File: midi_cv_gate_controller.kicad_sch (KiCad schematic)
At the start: 1 part, among them U28 ARDUINO_PRO_MINI

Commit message: Fixed alignment of jacks and LEDs
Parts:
- renumbered U28 to U122
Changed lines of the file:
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@@
   (symbol (lib_id "My Stuff:ARDUINO_PRO_MINI_custom_2") (at 119.38 93.98 0) (unit 1)
     (in_bom yes) (on_board yes) (fields_autoplaced)
-    (property "Reference" "U28" (id 0) (at 119.38 59.5335 0))
+    (property "Reference" "U122" (id 0) (at 119.38 59.5335 0))
     (property "Value" "ARDUINO_PRO_MINI" (id 1) (at 119.38 62.3086 0))
     (property "Footprint" "My Stuff:MODULE_ARDUINO_PRO_MINI_custom_2" (id 2) (at 98.044 52.832 0)

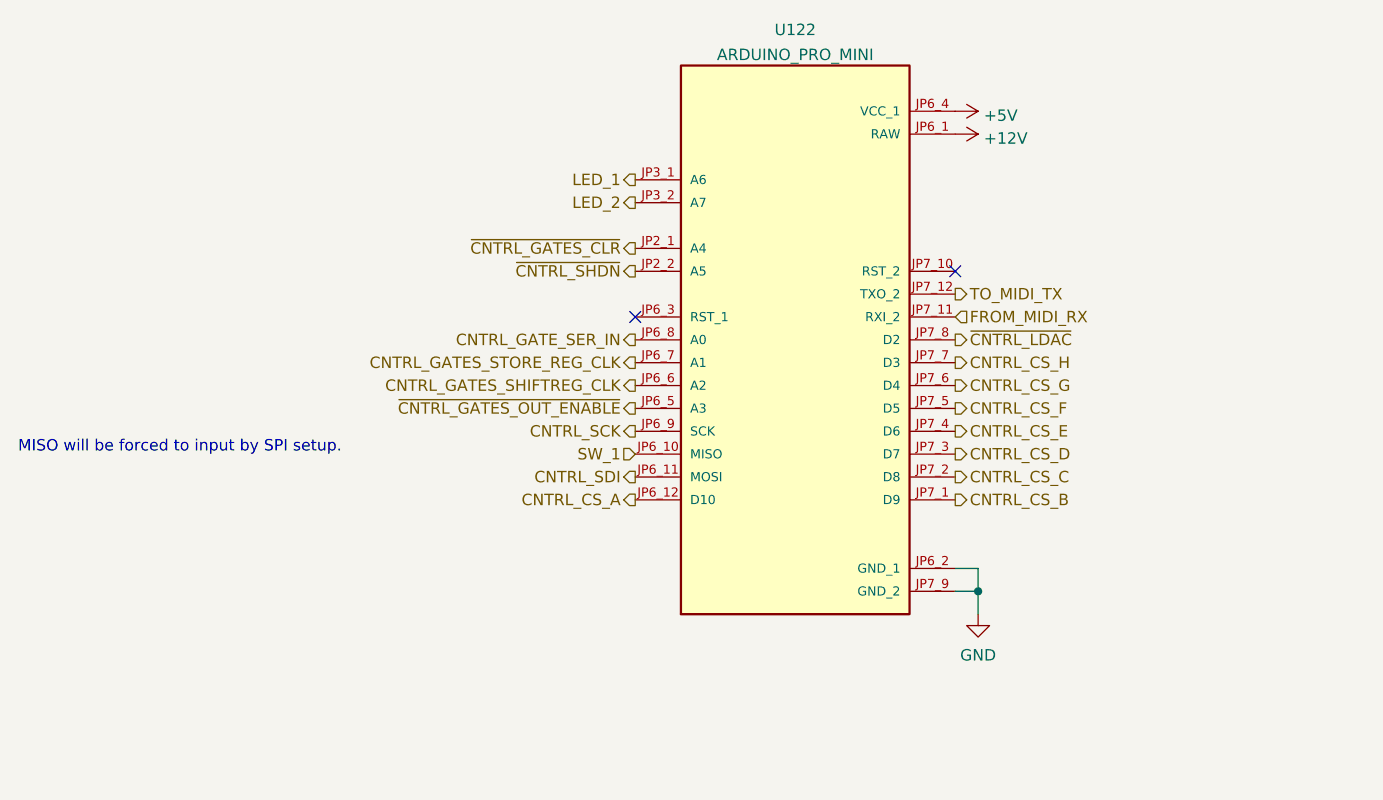
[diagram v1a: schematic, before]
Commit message: Cleanups and title blocks
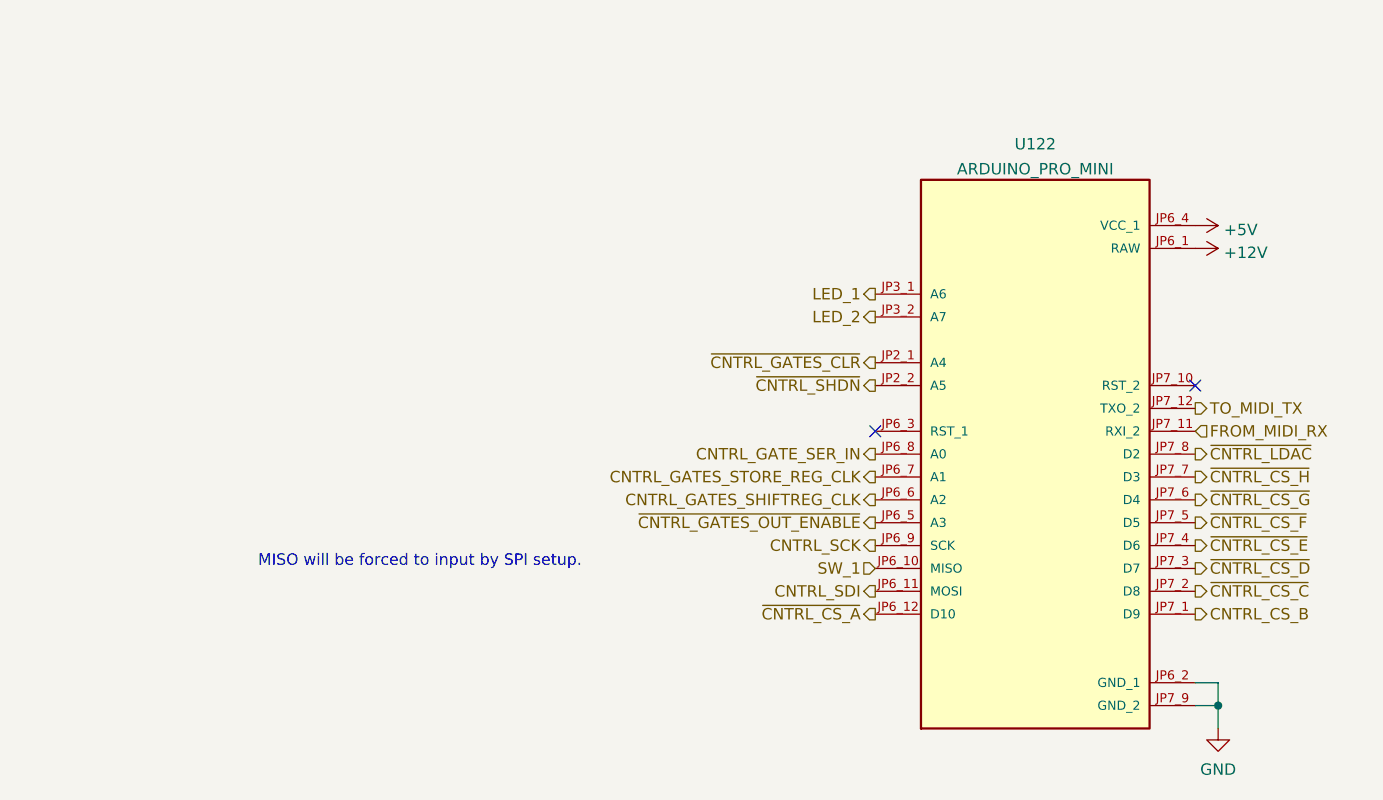
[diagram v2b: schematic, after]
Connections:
- net CNTRL_CS_A renamed ~{CNTRL_CS_A}
- net CNTRL_CS_B renamed ~{}CNTRL_CS_B
- net CNTRL_CS_C renamed ~{CNTRL_CS_C}
- net CNTRL_CS_D renamed ~{CNTRL_CS_D}
- net CNTRL_CS_E renamed ~{CNTRL_CS_E}
- net CNTRL_CS_F renamed ~{CNTRL_CS_F}
- net CNTRL_CS_G renamed ~{CNTRL_CS_G}
- net CNTRL_CS_H renamed ~{CNTRL_CS_H}
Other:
- company: (none) -> RobotDialogs
- title: (none) -> Eurorack MIDI 16x16 CV Gate
- moved on the sheet: U122
